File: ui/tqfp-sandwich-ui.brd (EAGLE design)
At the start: 87.3 x 57.1 mm, 40 parts, among them U1 MCP1754X-XXXXX/C, U3 MCP1754X-XXXXX/C

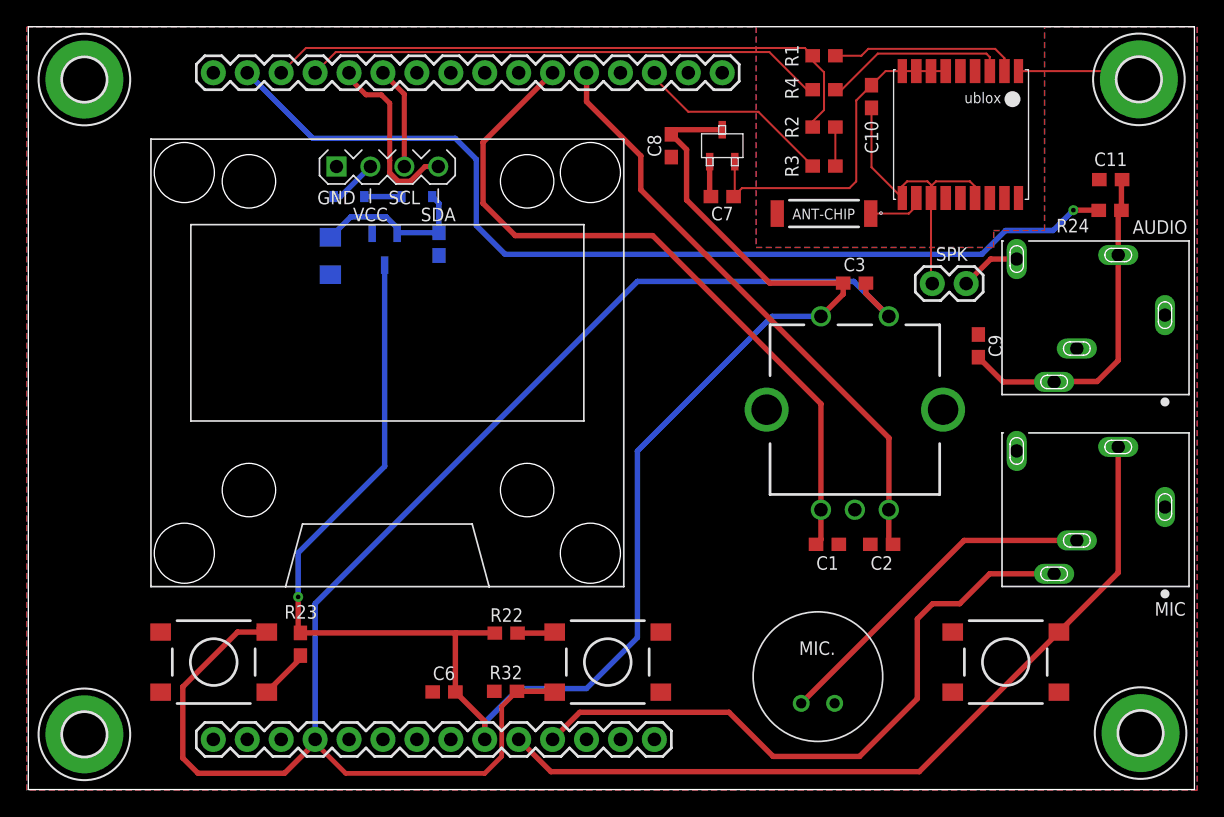
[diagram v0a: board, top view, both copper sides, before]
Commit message: GPS fix, Add LM386 (thanks Kris SQ3PCA)
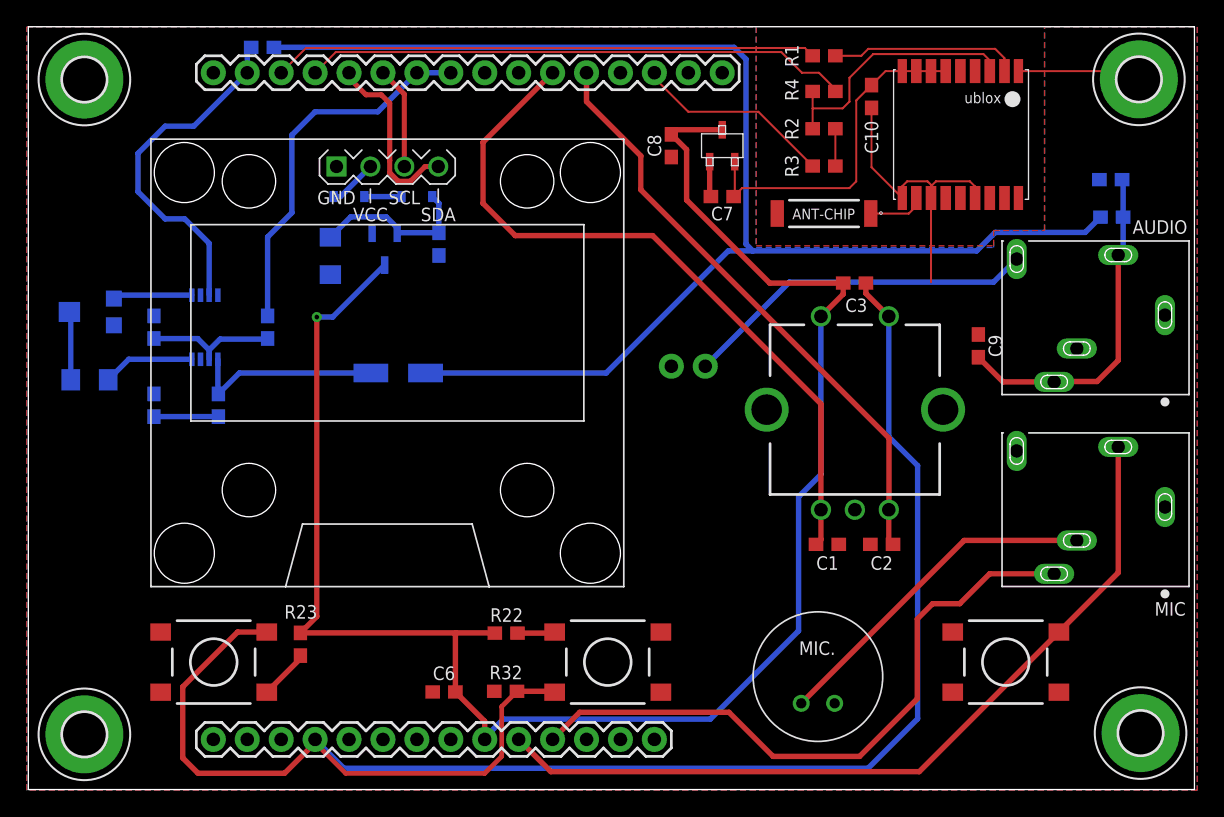
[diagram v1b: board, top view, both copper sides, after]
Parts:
- added C12: 47nF, SparkFun-Capacitors:0603
- added C13: 100nF, SparkFun-Capacitors:0603
- added C15: 220 uF, rcl:PANASONIC_C
- added C16: 10uF, SparkFun-Capacitors:EIA3216
- added IC2: LM386MM-1, linear:MMSOP08
- added R5, R6: 0, SparkFun-Resistors:0603
- added R9: 10, SparkFun-Resistors:0603
- added VR1: 10k, SparkFun-Resistors:TRIMPOT-SMD-TC33X
- R1: value 3.3k -> 0
- R4: value 0 -> 3.3k
- moved SPK 20.5 mm to (50.8, 31.8), flipped to the bottom, turned to 0 degrees
- moved R24 0.52 mm to (81.2, 42.9), flipped to the bottom, turned to 0 degrees
- moved R4 0.13 mm to (59.7, 52.3)
- moved R2 0.13 mm to (59.7, 49.5)
- flipped C11 to the bottom, turned to 180 degrees
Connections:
- new net +12V: J2.7, J2.8, R5.2
- new net N$11: C15.+, IC2.5, R9.2
- new net N$21: IC2.1, VR1.1
- new net N$22: C16.+, VR1.2
- new net N$23: C16.-, IC2.8
- new net N$24: C13.2, IC2.6, R5.1
- new net N$9: C12.1, R9.1
- new net SPK_AUDIO: C15.-, R24.2, R6.2
- net AUDIO: now also IC2.3, R6.1; no longer R24.2
- net GND: now also C12.2, C13.1, IC2.2, IC2.4
- net N$3: now also R2.1, R4.2; no longer R4.1
- net PD0_RXD: no longer R2.1
- net PD1_TXD: now also R4.1; no longer R4.2
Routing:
- net SPK_AUDIO: track 0.00 -> 105.6 mm
- net AUDIO: track 73.7 -> 26.4 mm, vias 1 -> 0
- net +12V: track 0.00 -> 28.1 mm
- net N$10: track 4.54 -> 26.6 mm
- net N$11: track 0.00 -> 14.7 mm
- net PC3_ADC3: track 117.4 -> 131.8 mm
- net N$24: track 0.00 -> 9.91 mm
- net N$23: track 0.00 -> 6.90 mm
- net PD0_RXD: track 46.9 -> 40.8 mm
- net N$21: track 0.00 -> 5.94 mm
- net N$3: track 13.8 -> 19.8 mm
- net N$22: track 0.00 -> 5.12 mm
- net N$9: track 0.00 -> 4.83 mm
- net VCC: track 127.8 -> 132.3 mm
- net PD1_TXD: track 39.6 -> 40.9 mm
- removed copper zone on layer 15, net GND
- removed copper zone on layer 2, net GND
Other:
- board text added: "AUDIO AMPLIFIER"
- board text added: "DO NOT INSTALL ->"
- board text added: "GPS"
- board text added: "OLED - GPS DL2MAN UI Compatible Rev. D"
- board text added: "OPTIONAL"
- board text added: "TO BYPASS INSTALL R6"
- board text removed: "OLED - GPS DL2MAN UI Compatible Rev. C"
